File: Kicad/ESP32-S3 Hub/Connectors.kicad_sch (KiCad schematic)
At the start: 23 parts, among them J1 1.27mm 3pin socket, J10 1.27mm 3pin socket, J11 7 pin FPC 0.3mm Panasonic Y3b, J12 1.27mm 3pin socket, J13 Molex 2167000249 SlimStack re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, J14 Molex 2167000249 SlimStack pl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, J15 Molex 2167000249 SlimStack pl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, J2 1.27mm 3pin socket, J20 Molex 2167000249 SlimStack re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, J21 1.27mm 4 pin socket, J22 1.27mm 4 pin header, J3 7 pin FPC 0.3mm Panasonic Y3b, J4 1.27mm 3pin socket, J5 7 pin FPC 0.3mm Panasonic Y3b, J6 1.27mm 3pin socket, J7 1.27mm 3pin socket, J8 7 pin FPC 0.3mm Panasonic Y3b, J9 1.27mm 3pin socket

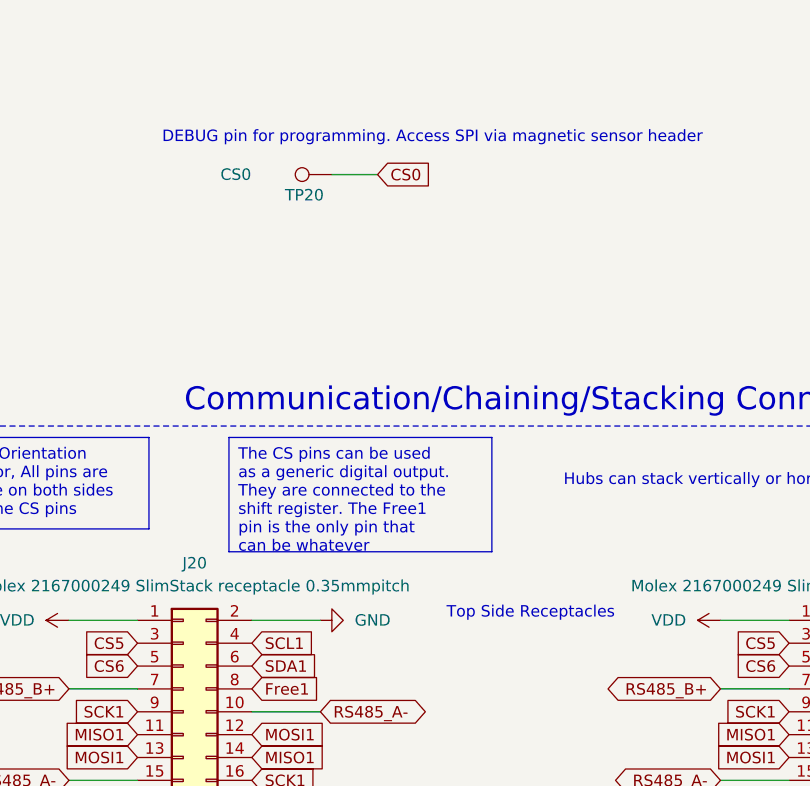
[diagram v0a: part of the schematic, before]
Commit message: Fixed ERC errors, stopped tracking a few .obsidian files
The only errors that popped up were the dual labeling of CS0 and Uart RTS, a power flag spot, and a modified footprint error.
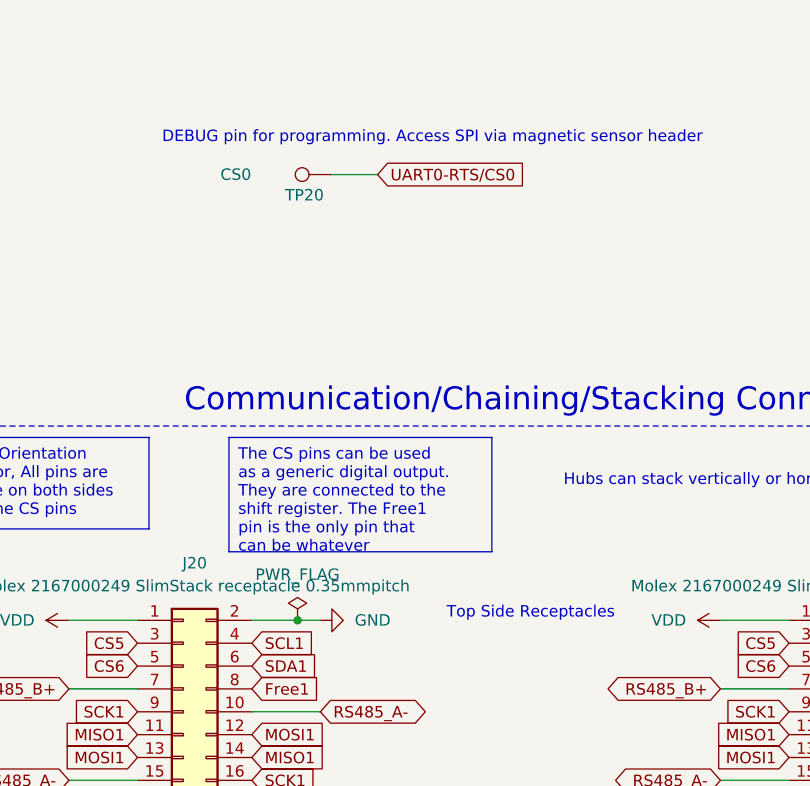
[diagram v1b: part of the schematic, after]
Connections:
- net CS0 renamed UART0-RTS/CS0
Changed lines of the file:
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@@
 	)
 	(junction
+		(at 186.69 85.09)
+		(diameter 0)
+		(color 0 0 0 0)
+	)
+	(junction
 		(at 69.85 102.87)
 		(diameter 0)
@@
 	(wire
 		(pts
-			(xy 189.23 85.09) (xy 181.61 85.09)
+			(xy 189.23 85.09) (xy 186.69 85.09)
 		)
 		(stroke
@@
 	(wire
 		(pts
+			(xy 186.69 85.09) (xy 181.61 85.09)
+		)
+		(stroke
+			(width 0)
+			(type default)
+		)
+	)
+	(wire
+		(pts
 			(xy 233.68 138.43) (xy 241.3 138.43)
 		)
@@
 		)
 	)
-	(global_label "CS0"
-		(shape input)
-		(at 195.58 35.56 0)
-		(fields_autoplaced yes)
-		(effects
-			(font
-				(size 1.27 1.27)
-			)
-			(justify left)
-		)
-		(property "Intersheetrefs" "${INTERSHEET_REFS}"
-			(at 202.2542 35.56 0)
-			(effects
-				(font
-					(size 1.27 1.27)
-				)
-				(justify left)
-				(hide yes)
-			)
-		)
-	)
 	(global_label "SCK1"
 		(shape input)
@@
 		)
 	)
+	(global_label "UART0-RTS{slash}CS0"
+		(shape input)
+		(at 195.58 35.56 0)
+		(fields_autoplaced yes)
+		(effects
+			(font
+				(size 1.27 1.27)
+			)
+			(justify left)
+		)
+		(property "Intersheetrefs" "${INTERSHEET_REFS}"
+			(at 214.4704 35.56 0)
+			(effects
+				(font
+					(size 1.27 1.27)
+				)
+				(justify left)
+				(hide yes)
+			)
+		)
+	)
 	(global_label "3C"
 		(shape input)
@@
 					(unit 1)
 				)
+			)
+		)
+	)
+	(symbol
+		(lib_id "power:PWR_FLAG")
+		(at 186.69 85.09 0)
+		(unit 1)
+		(exclude_from_sim no)
+		(in_bom yes)
+		(on_board yes)
+		(dnp no)
+		(fields_autoplaced yes)
+		(property "Reference" "#FLG03"
+			(at 186.69 83.185 0)
+			(effects
+				(font
+					(size 1.27 1.27)
+				)
+				(hide yes)
+			)
+		)
+		(property "Value" "PWR_FLAG"
+			(at 186.69 80.01 0)
+			(effects
+				(font
+					(size 1.27 1.27)
+				)
+			)
+		)
+		(property "Footprint" ""
+			(at 186.69 85.09 0)
+			(effects
+				(font
+					(size 1.27 1.27)
+				)
+				(hide yes)
+			)
+		)
+		(property "Datasheet" "~"
+			(at 186.69 85.09 0)
+			(effects
+				(font
+					(size 1.27 1.27)
+				)
+				(hide yes)
+			)
+		)
+		(property "Description" "Special symbol for telling ERC where power comes from"
+			(at 186.69 85.09 0)
+			(effects
+				(font
+					(size 1.27 1.27)
+				)
+				(hide yes)
+			)
+		)
+		(pin "1"
+		)
+		(instances
+			(project "ESP32-S3 Hub"
+				(path "/a8c80fba-3bca-4358-b5bb-9ebf9383c658/e098af34-1b04-4f22-87f1-2a3ef3b390de"
+					(reference "#FLG03")
+					(unit 1)
+				)

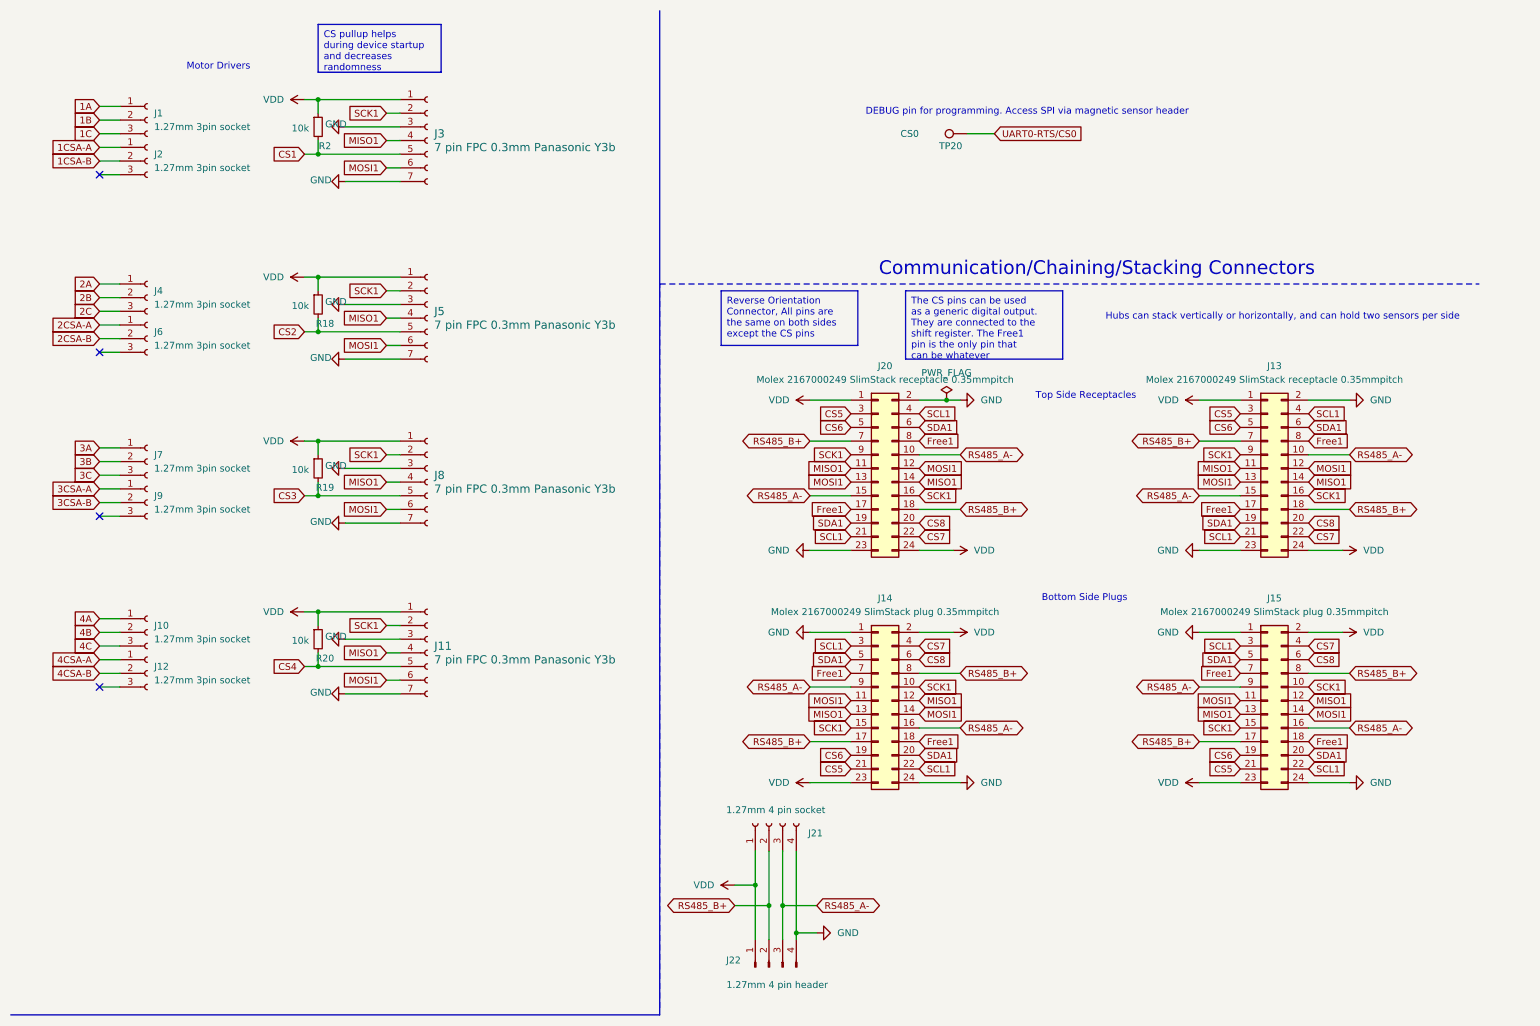
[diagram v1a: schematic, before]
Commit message: Switched out Mezzanine Connectors
I'm going with some 30-pin TE mezzanine connectors, which are cheaper than before and have a few extra pins if I need them in the future.
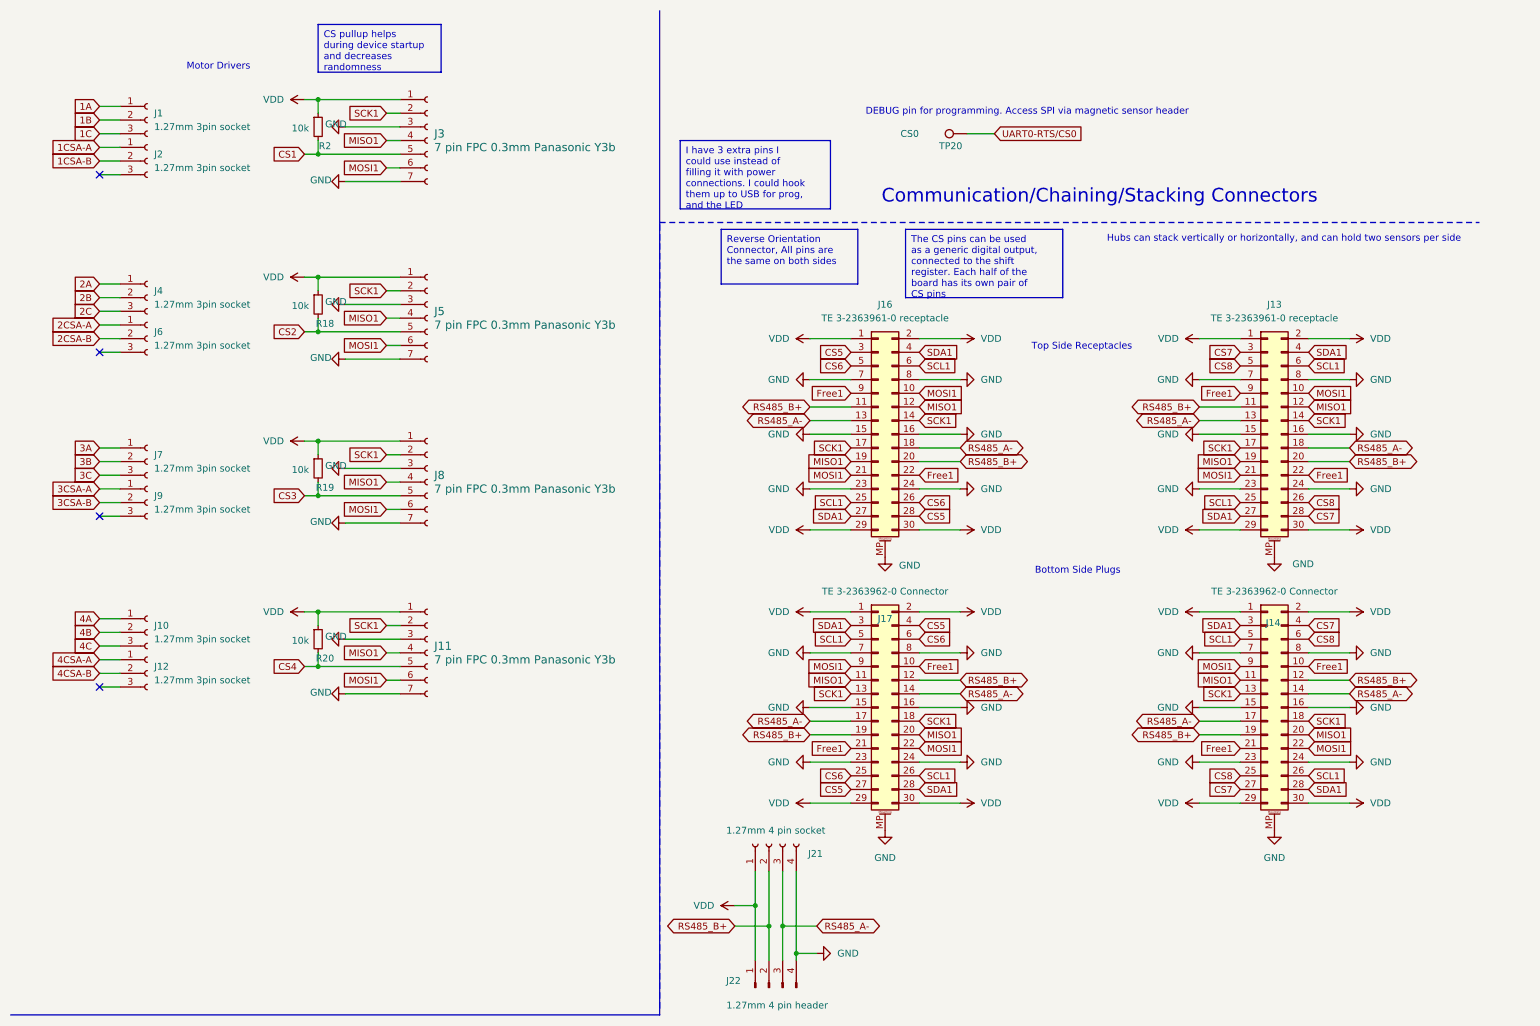
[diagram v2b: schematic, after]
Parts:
- removed J13, J20: Molex 2167000249 SlimStack receptacle 0.35mmpitch, symbol Connector_Generic:Conn_02x12_Odd_Even
- removed J14, J15: Molex 2167000249 SlimStack plug 0.35mmpitch, symbol Connector_Generic:Conn_02x12_Odd_Even
- added J13, J16: TE 3-2363961-0 receptacle, custom_testpoints:TE_mezzanine_rec_3-2363961-0, symbol Connector_Generic_MountingPin:Conn_02x15_Odd_Even_MountingPin
- added J14, J17: TE 3-2363962-0 Connector, custom_testpoints:TE_mezzanine_conn_3-2363962-0, symbol Connector_Generic_MountingPin:Conn_02x15_Odd_Even_MountingPin
- J21: footprint (none) -> Connector_PinSocket_1.27mm:PinSocket_1x04_P1.27mm_Vertical
- J22: footprint (none) -> Connector_PinHeader_1.27mm:PinHeader_1x04_P1.27mm_Horizontal
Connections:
- net CS5: now also J16.28 (Pin_28), J16.3 (Pin_3), J17.27 (Pin_27), J17.4 (Pin_4)
- net CS6: now also J16.26 (Pin_26), J16.5 (Pin_5), J17.25 (Pin_25), J17.6 (Pin_6)
- net CS7: now also J13.28 (Pin_28), J13.3 (Pin_3), J14.27 (Pin_27), J14.4 (Pin_4)
- net CS8: now also J13.26 (Pin_26), J13.5 (Pin_5), J14.25 (Pin_25), J14.6 (Pin_6)
- net Free1: now also J13.22 (Pin_22), J13.9 (Pin_9), J14.10 (Pin_10), J14.21 (Pin_21), J16.22 (Pin_22), J16.9 (Pin_9), J17.10 (Pin_10), J17.21 (Pin_21)
- net GND: now also J13.15 (Pin_15), J13.16 (Pin_16), J13.23 (Pin_23), J13.24 (Pin_24), J13.7 (Pin_7), J13.8 (Pin_8), J13.MP (MountPin), J14.15 (Pin_15), J14.16 (Pin_16), J14.23 (Pin_23), J14.24 (Pin_24), J14.7 (Pin_7), J14.8 (Pin_8), J14.MP (MountPin), J16.15 (Pin_15), J16.16 (Pin_16), J16.23 (Pin_23), J16.24 (Pin_24), J16.7 (Pin_7), J16.8 (Pin_8), J16.MP (MountPin), J17.15 (Pin_15), J17.16 (Pin_16), J17.23 (Pin_23), J17.24 (Pin_24), J17.7 (Pin_7), J17.8 (Pin_8), J17.MP (MountPin)
- net MISO1: now also J13.12 (Pin_12), J13.19 (Pin_19), J14.11 (Pin_11), J14.20 (Pin_20), J16.12 (Pin_12), J16.19 (Pin_19), J17.11 (Pin_11), J17.20 (Pin_20)
- net MOSI1: now also J13.10 (Pin_10), J13.21 (Pin_21), J14.22 (Pin_22), J14.9 (Pin_9), J16.10 (Pin_10), J16.21 (Pin_21), J17.22 (Pin_22), J17.9 (Pin_9)
- net RS485_A-: now also J13.13 (Pin_13), J13.18 (Pin_18), J14.14 (Pin_14), J14.17 (Pin_17), J16.13 (Pin_13), J16.18 (Pin_18), J17.14 (Pin_14), J17.17 (Pin_17)
- net RS485_B+: now also J13.11 (Pin_11), J13.20 (Pin_20), J14.12 (Pin_12), J14.19 (Pin_19), J16.11 (Pin_11), J16.20 (Pin_20), J17.12 (Pin_12), J17.19 (Pin_19)
- net SCK1: now also J13.14 (Pin_14), J13.17 (Pin_17), J14.13 (Pin_13), J14.18 (Pin_18), J16.14 (Pin_14), J16.17 (Pin_17), J17.13 (Pin_13), J17.18 (Pin_18)
- net SCL1: now also J13.25 (Pin_25), J13.6 (Pin_6), J14.26 (Pin_26), J14.5 (Pin_5), J16.25 (Pin_25), J16.6 (Pin_6), J17.26 (Pin_26), J17.5 (Pin_5)
- net SDA1: now also J13.27 (Pin_27), J13.4 (Pin_4), J14.28 (Pin_28), J14.3 (Pin_3), J16.27 (Pin_27), J16.4 (Pin_4), J17.28 (Pin_28), J17.3 (Pin_3)
- net VDD: now also J13.1 (Pin_1), J13.2 (Pin_2), J13.29 (Pin_29), J13.30 (Pin_30), J14.1 (Pin_1), J14.2 (Pin_2), J14.29 (Pin_29), J14.30 (Pin_30), J16.1 (Pin_1), J16.2 (Pin_2), J16.29 (Pin_29), J16.30 (Pin_30), J17.1 (Pin_1), J17.2 (Pin_2), J17.29 (Pin_29), J17.30 (Pin_30)
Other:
- moved on the sheet: J21, J22

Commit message: Switching out footprints for smaller variants, dropping rs485 resistors
Space is tight, so I had to downsize the crystal and the reset switches. I also don't have space for the rs485 termination resistors configurable per device, so I have excluded this from the board.
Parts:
- R18, R19, R2, R20: footprint Resistor_SMD:R_0603_1608Metric -> Resistor_SMD:R_0402_1005Metric
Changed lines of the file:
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@@
 			)
 		)
-		(property "Footprint" "Resistor_SMD:R_0603_1608Metric"
+		(property "Footprint" "Resistor_SMD:R_0402_1005Metric"
 			(at 69.85 129.54 0)
 			(effects
@@
 			)
 		)
-		(property "Footprint" "Resistor_SMD:R_0603_1608Metric"
+		(property "Footprint" "Resistor_SMD:R_0402_1005Metric"
 			(at 69.85 97.79 0)
 			(effects
@@
 			)
 		)
-		(property "Footprint" "Resistor_SMD:R_0603_1608Metric"
+		(property "Footprint" "Resistor_SMD:R_0402_1005Metric"
 			(at 69.85 67.31 0)
 			(effects
@@
 			)
 		)
-		(property "Footprint" "Resistor_SMD:R_0603_1608Metric"
+		(property "Footprint" "Resistor_SMD:R_0402_1005Metric"
 			(at 69.85 34.29 0)
 			(effects

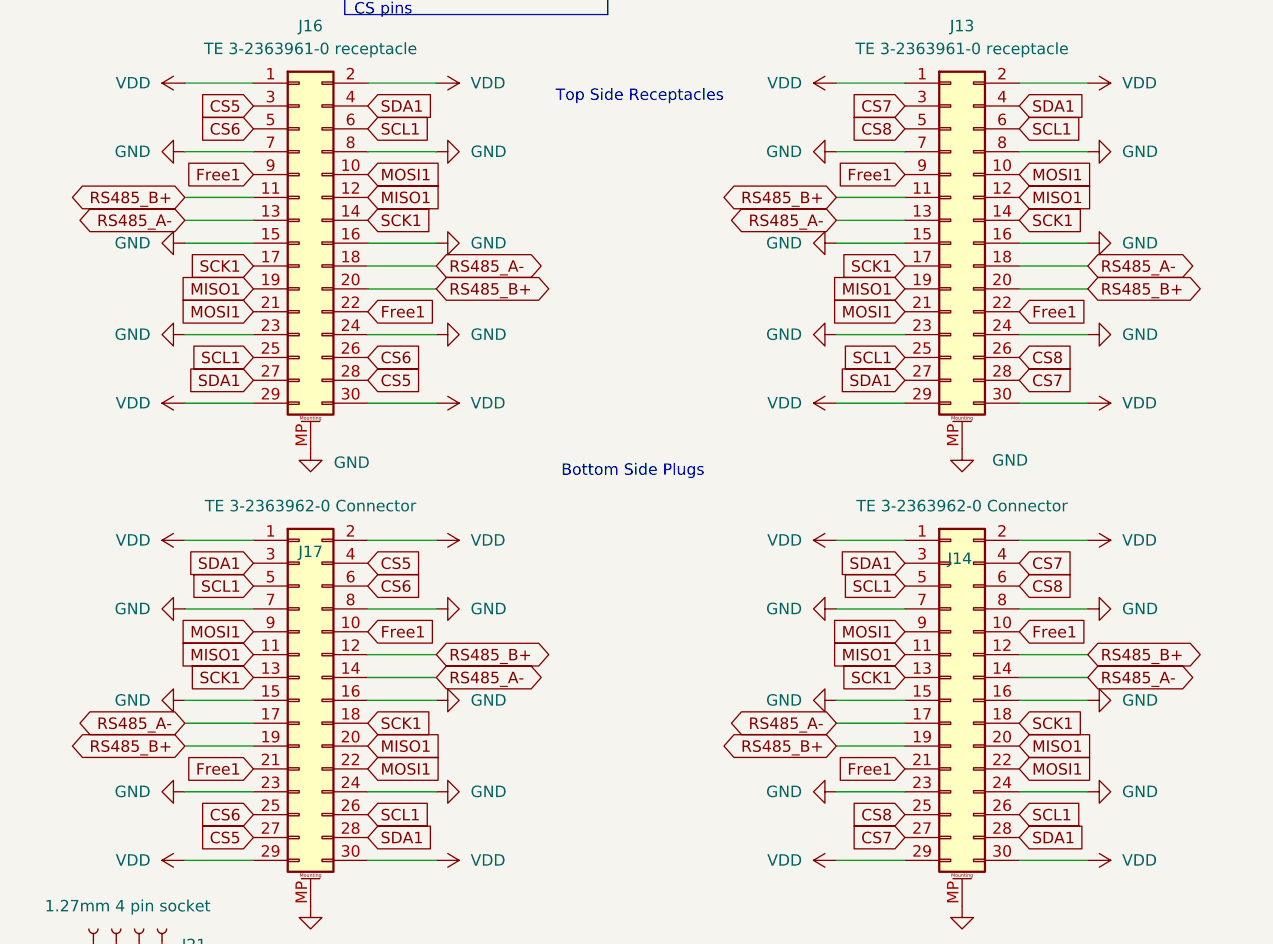
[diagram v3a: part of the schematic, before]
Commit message: Finished basic layout
Everything is crammed in there, I do have some extras bit of space up top for an extra component or two. I probably should take advantage of that space somehow. For routing this thing, I really think i need a 6 or 8 layer board with blind vias.
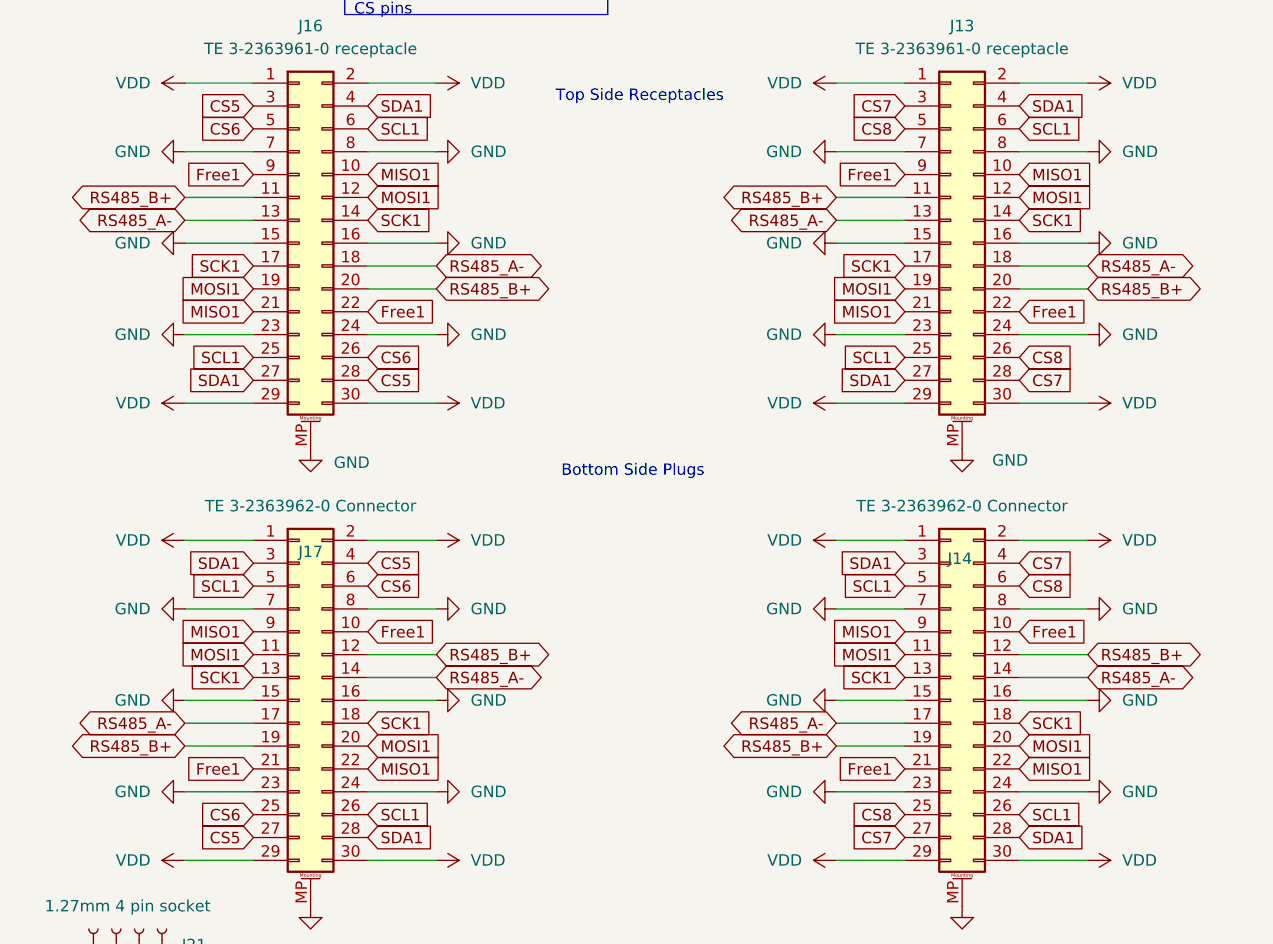
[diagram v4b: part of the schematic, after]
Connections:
- net MISO1: now also J13.10 (Pin_10), J13.21 (Pin_21), J14.22 (Pin_22), J14.9 (Pin_9), J16.10 (Pin_10), J16.21 (Pin_21), J17.22 (Pin_22), J17.9 (Pin_9); no longer J13.12 (Pin_12), J13.19 (Pin_19), J14.11 (Pin_11), J14.20 (Pin_20), J16.12 (Pin_12), J16.19 (Pin_19), J17.11 (Pin_11), J17.20 (Pin_20)
- net MOSI1: now also J13.12 (Pin_12), J13.19 (Pin_19), J14.11 (Pin_11), J14.20 (Pin_20), J16.12 (Pin_12), J16.19 (Pin_19), J17.11 (Pin_11), J17.20 (Pin_20); no longer J13.10 (Pin_10), J13.21 (Pin_21), J14.22 (Pin_22), J14.9 (Pin_9), J16.10 (Pin_10), J16.21 (Pin_21), J17.22 (Pin_22), J17.9 (Pin_9)
